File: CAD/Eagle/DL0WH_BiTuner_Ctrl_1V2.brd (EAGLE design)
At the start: 96.5 x 73 mm, 157 parts, among them Q0321 ABS07-32.768KHZ, U0101 STM32L476RXT_64PIN_LDO, U0601 MC33996, U0701 MC33996, U0801 MC33996, U0921 TS5A23166, U0941 LM2611, U0951 OPA354, U0961 OPA354, U0962 MCP4661-103E-MS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

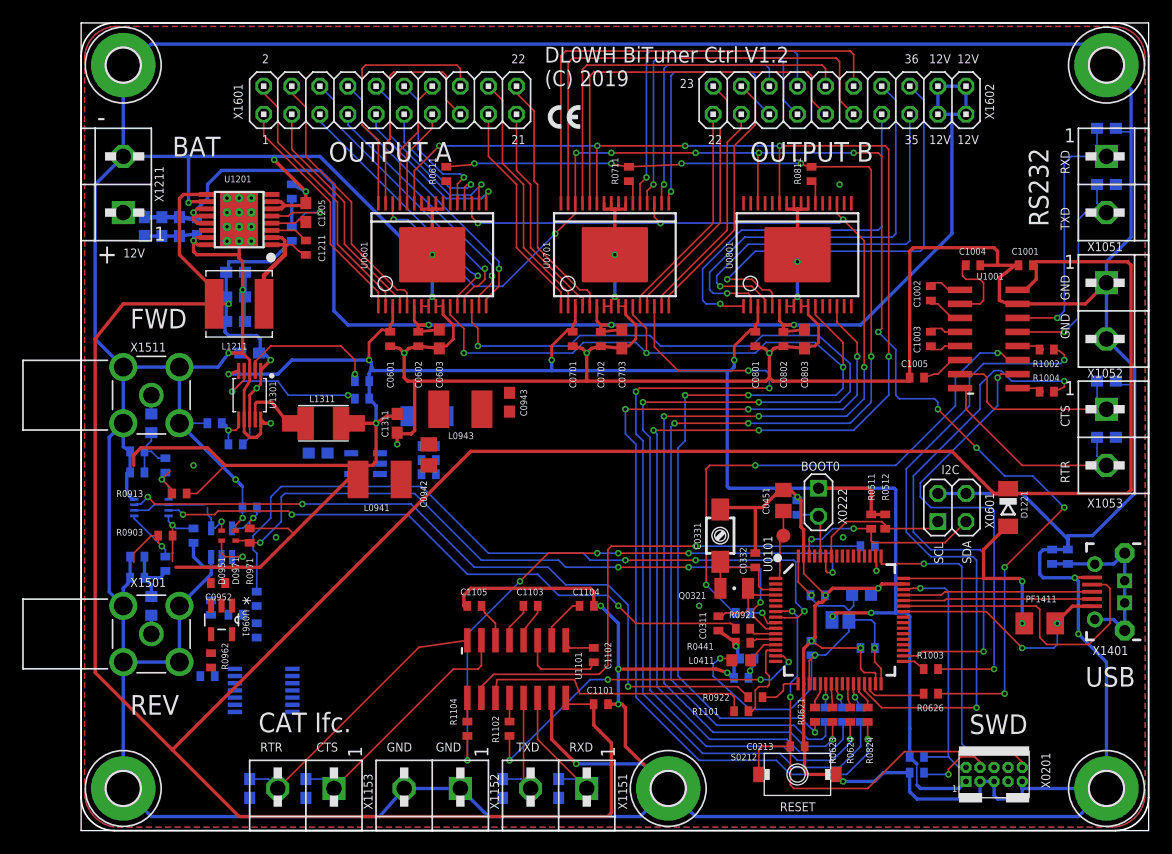
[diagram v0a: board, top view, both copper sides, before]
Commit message: HW_1V2 - CAD/Eagle/lbr - df4iah_connector SWD-connector restring change
Signed-off-by: Ulrich Habel <espero7757@gmx.net>
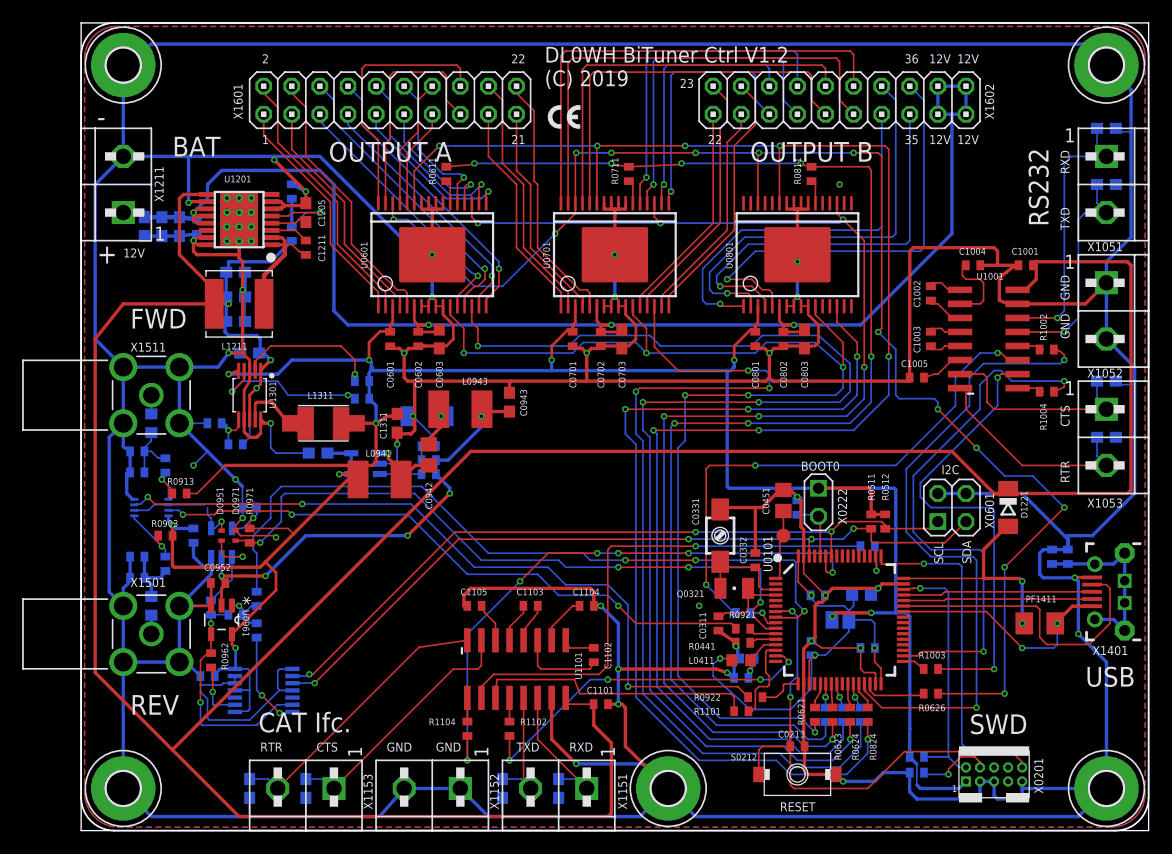
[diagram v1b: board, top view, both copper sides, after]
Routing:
- net PB6: track 12.7 -> 67.2 mm, vias 0 -> 3
- net PB9: track 17.9 -> 70.3 mm, vias 2 -> 4
- net GND: track 854.6 -> 902.4 mm
- net -1V5: track 0.00 -> 41.5 mm, vias 0 -> 5
- net SWR_OP2_IN: track 0.00 -> 21.1 mm, vias 0 -> 2
- net +3V3: track 220.2 -> 240.7 mm, vias 9 -> 11
- net OPA_FB: track 0.00 -> 9.04 mm, vias 0 -> 2
- net LM2611_SW: track 0.00 -> 6.48 mm, vias 0 -> 1
- net LM2611_NFB: track 0.00 -> 6.31 mm
- net OPA_PULL: track 0.00 -> 5.43 mm, vias 0 -> 1
- net SWR_OP2_OUT: track 0.00 -> 4.74 mm, vias 0 -> 1
- net LM_DA: track 0.00 -> 4.71 mm, vias 0 -> 1
- net SWR_IN_FWD: track 9.64 -> 5.94 mm
- net SWR_OP1_OUT: track 5.38 -> 8.86 mm
- net SWR_IN_REV: track 5.50 -> 4.45 mm
